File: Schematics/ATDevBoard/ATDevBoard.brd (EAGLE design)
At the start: 75.9 x 57.1 mm, 42 parts, among them U1 TINY85-20-DIP

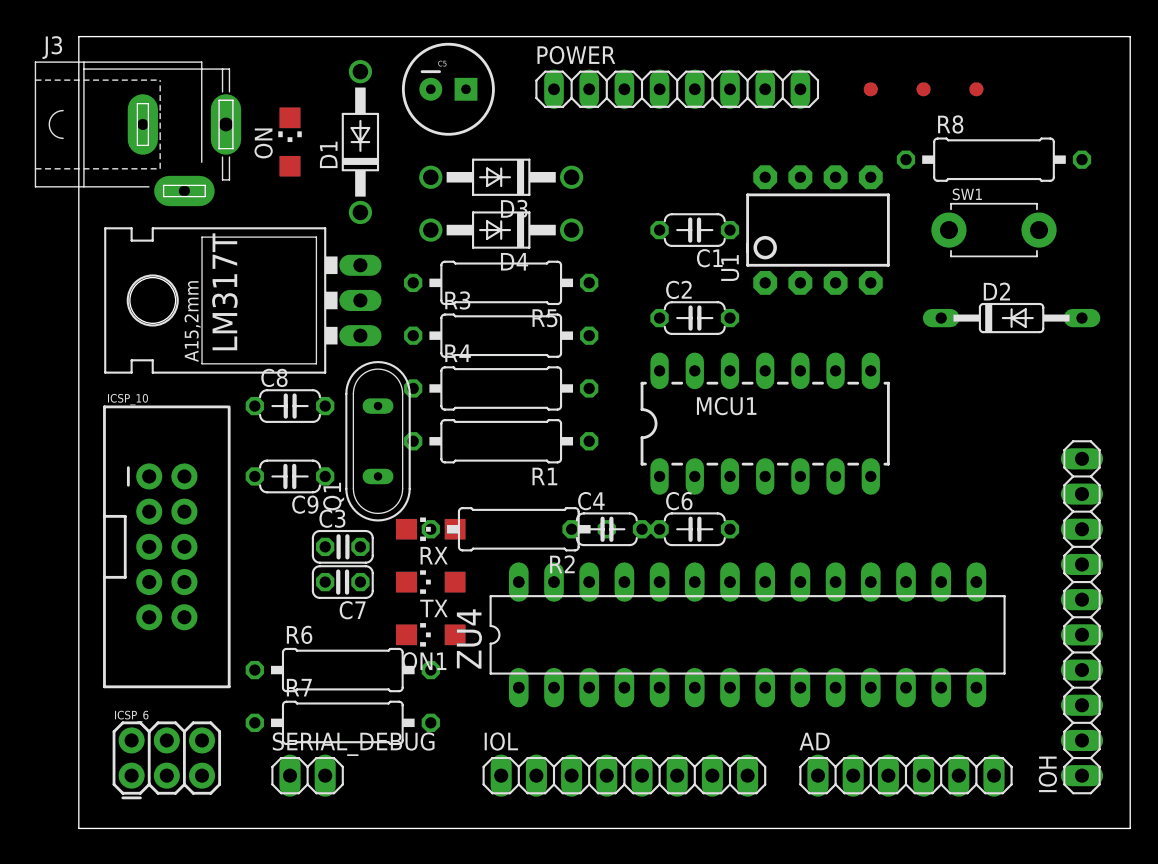
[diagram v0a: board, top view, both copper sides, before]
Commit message: Added vaule for regulator resistors, first routed version of brd. Added pdfs for brd and schematic.
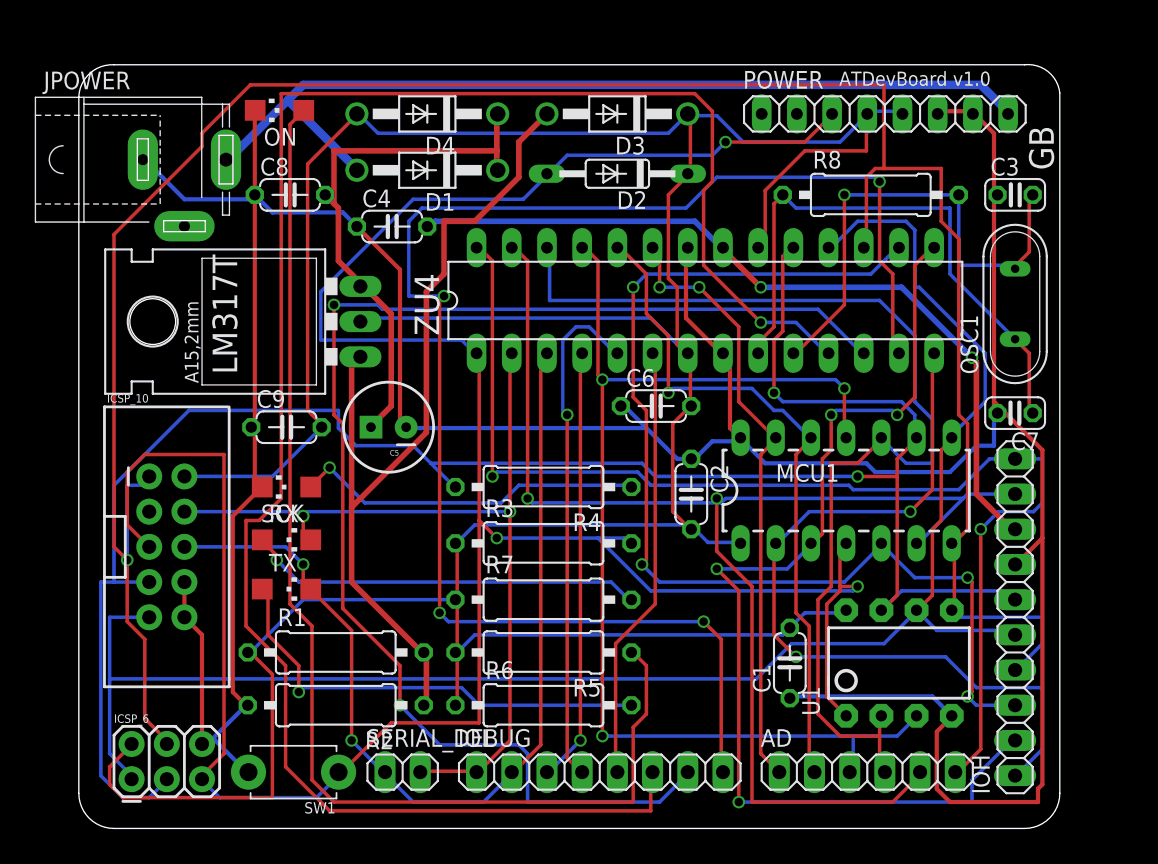
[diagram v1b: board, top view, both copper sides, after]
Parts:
- removed FD1, FD2, FD3: FIDUCIALMOUNT, SmartPrj:FIDUCIA-MOUNT
- removed J3: (no value), con-jack:SPC4077
- removed ON1: BLUE, led:CHIPLED_1206
- removed Q1: (no value), special:QS
- added JPOWER: (no value), con-jack:SPC4077
- added OSC1: (no value), special:QS
- added SCK: BLUE, led:CHIPLED_1206
- R1: value (none) -> 5K6
- R2: value 1M -> 10K
- R4: value (none) -> 1K
- R8: value 1K -> 1M
- moved SW1 63.9 mm to (15.5, 4.06), turned to 180 degrees
- moved C3 54.8 mm to (67.6, 45.7)
- moved C7 50.0 mm to (67.6, 30.0)
- moved C1 32.0 mm to (51.3, 11.9), turned to 90 degrees
- moved U1 31.8 mm to (59.2, 11.9)
- moved D2 30.3 mm to (38.9, 47.2), turned to 180 degrees
- moved R5 26.8 mm to (33.5, 12.7)
- moved C4 26.8 mm to (22.6, 43.4)
- moved C5 24.8 mm to (22.4, 29.0), turned to 180 degrees
- moved ZU4 24.3 mm to (45.2, 38.1)
- moved R1 19.4 mm to (18.5, 12.7), turned to 0 degrees
- moved R2 18.3 mm to (18.5, 8.89)
- moved R7 17.0 mm to (33.5, 16.5)
- moved R3 15.3 mm to (33.5, 20.6)
- moved C8 15.2 mm to (15.2, 45.7)
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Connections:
- net +3V3: now also R1.1, R5.2, R6.1; no longer R4.1, R6.2, R8.1
- net GND: now also JPOWER.1, R2.2, SCK.C; no longer J3.1, ON1.C, R1.2
- net N$1: now also R1.2, R2.1; no longer R1.1, R4.2
- net N$3: now also R5.1; no longer R6.1
- net N$35: now also R7.2; no longer R8.2
- net N$36: now also R6.2; no longer R7.2
- net N$4: now also R4.1, SCK.A; no longer ON1.A, R5.1
- net SCK: now also R4.2; no longer R5.2
- net VIN: now also JPOWER.3; no longer J3.3
- net XTAL1: now also OSC1.1, R8.1; no longer Q1.1, R2.1
- net XTAL2: now also OSC1.2, R8.2; no longer Q1.2, R2.2
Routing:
- net +3V3: track 0.00 -> 258.4 mm
- net GND: track 0.00 -> 250.8 mm
- net RESET: track 0.00 -> 191.8 mm, vias 0 -> 3
- net MOSI: track 0.00 -> 167.9 mm, vias 0 -> 1
- net SCK: track 0.00 -> 142.1 mm, vias 0 -> 2
- net IO5: track 0.00 -> 136.5 mm, vias 0 -> 1
- net MISO: track 0.00 -> 122.5 mm
- net IO7: track 0.00 -> 110.2 mm, vias 0 -> 4
- net IO6: track 0.00 -> 97.2 mm, vias 0 -> 2
- net AD4: track 0.00 -> 95.3 mm, vias 0 -> 2
- net AD5: track 0.00 -> 85.2 mm, vias 0 -> 2
- net N$3: track 0.00 -> 84.9 mm
- net AD2: track 0.00 -> 83.4 mm, vias 0 -> 3
- net SS: track 0.00 -> 79.7 mm, vias 0 -> 4
- net AD3: track 0.00 -> 77.9 mm
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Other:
- board size 75.9 x 57.1 mm -> 70.8 x 55.1 mm
- board text added: "ATDevBoard v1.0"
- board text added: "GB"

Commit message: Fixed packages for some resistors, replaced 1N4004 with 1N4007 diodes
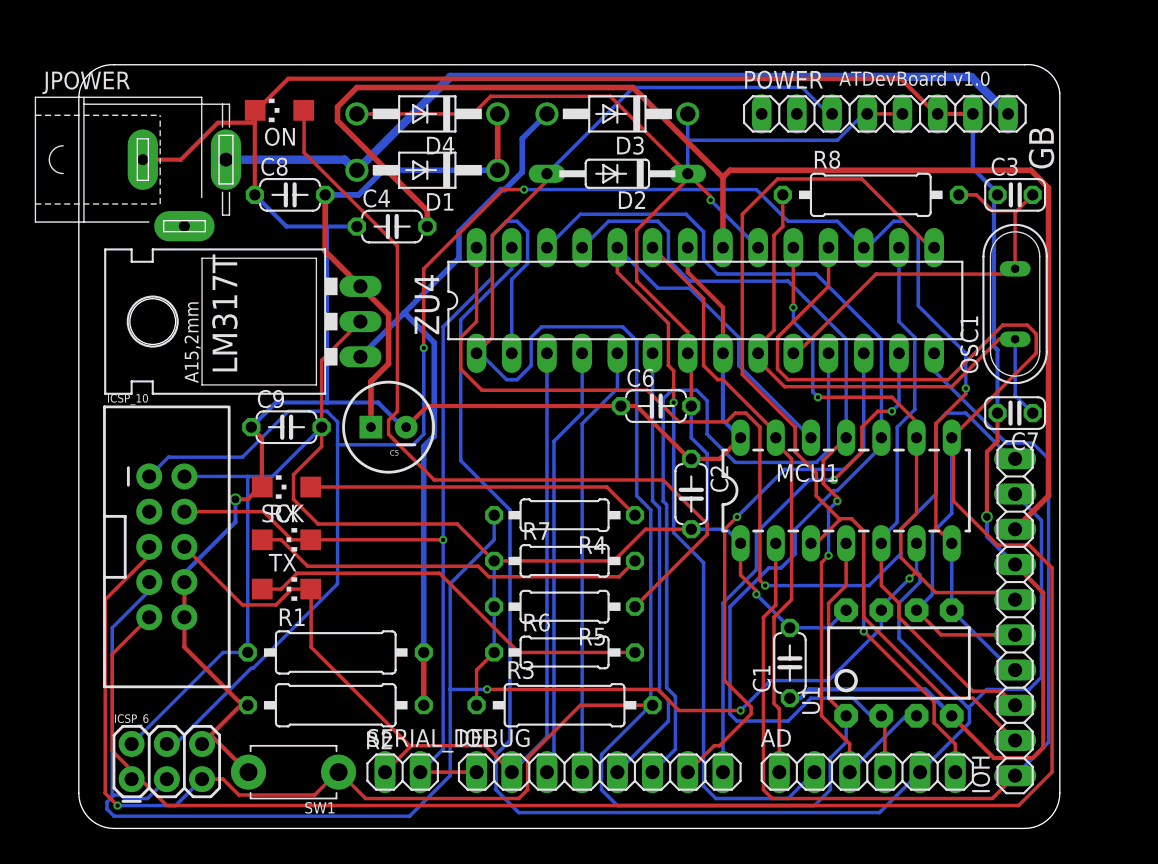
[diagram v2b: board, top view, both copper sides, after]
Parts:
- D3, D4: value 1N4004 -> 1N4007
- R4, R5, R6, R7: device rcl:0309/12 -> rcl:0207/10
- moved R3 11.8 mm to (35.1, 8.89)
- moved R6 4.10 mm to (35.1, 12.7)
- moved R5 3.64 mm to (35.1, 16.0)
- moved R7 3.18 mm to (35.1, 19.3)
- moved R4 2.54 mm to (35.1, 22.6)
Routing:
- net IO5: track 136.5 -> 51.1 mm, vias 1 -> 0
- net IO7: track 110.2 -> 37.1 mm, vias 4 -> 2
- net +3V3: track 258.4 -> 192.7 mm, vias 0 -> 2
- net IO6: track 97.2 -> 39.8 mm, vias 2 -> 1
- net MISO: track 122.5 -> 172.7 mm
- net SS: track 79.7 -> 39.7 mm, vias 4 -> 0
- net AREF: track 57.5 -> 97.3 mm, vias 2 -> 0
- net MOSI: track 167.9 -> 140.3 mm, vias 1 -> 3
- net N$3: track 84.9 -> 60.2 mm
- net AD1: track 49.1 -> 71.4 mm
- net AD4: track 95.3 -> 116.0 mm, vias 2 -> 0
- net AD2: track 83.4 -> 64.7 mm, vias 3 -> 2
- net IO0: track 61.2 -> 77.0 mm, vias 2 -> 1
- net IO8: track 57.6 -> 73.3 mm, vias 2 -> 0
- net N$1: track 63.5 -> 52.8 mm
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
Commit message: Fixed some components package with buy info, revisited board layout.
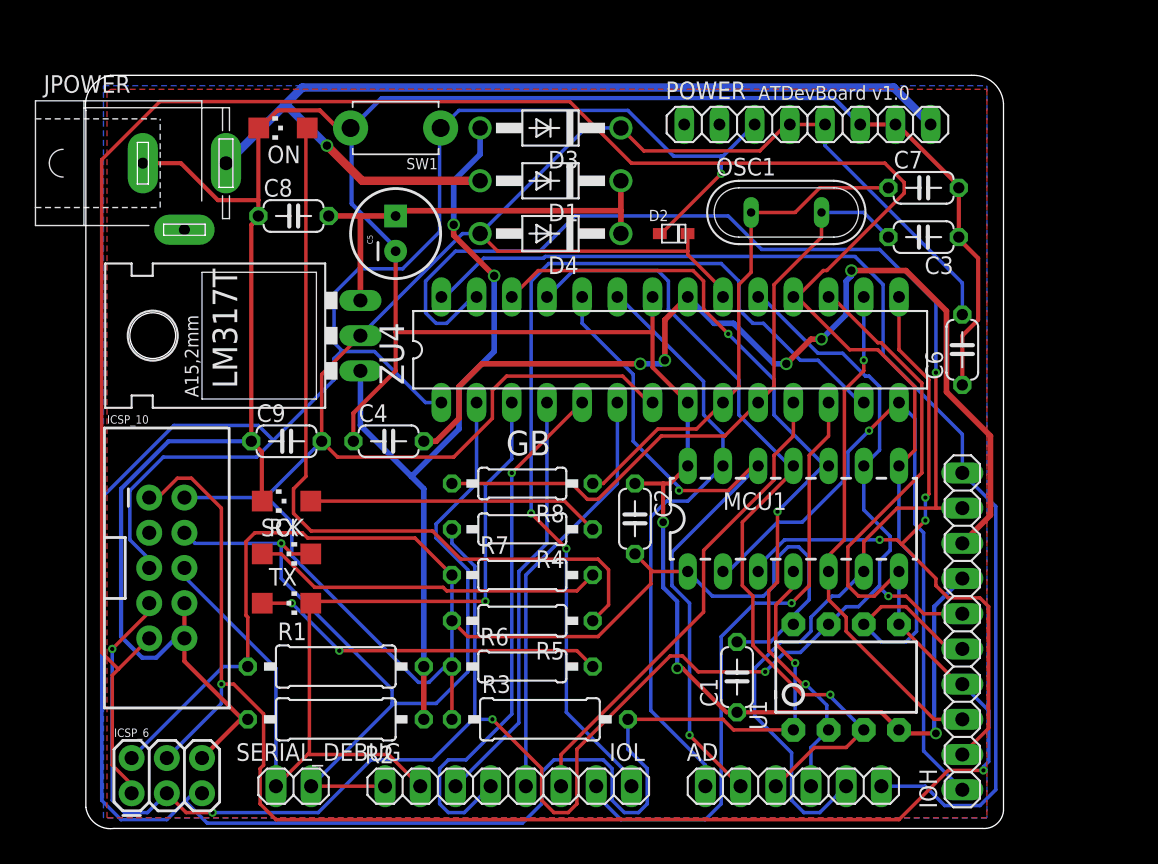
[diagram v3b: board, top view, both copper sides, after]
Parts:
- C3, C7: device SmartPrj:C025-024X044 -> SmartPrj:C050-024X044
- D2: device diode:DO35-10 -> adafruit:SOD-323F
- MCU1: value ATTINY84ATTINY84-20PU -> ATTINY84-20PU
- R8: device rcl:0309/12 -> rcl:0207/10
- U1: value TINY85-20-DIP -> TINY85-DIP
- moved SW1 47.1 mm to (22.9, 50.5)
- moved R8 32.7 mm to (32.0, 24.9), turned to 180 degrees
- moved C6 22.5 mm to (63.8, 34.5), turned to 90 degrees
- moved OSC1 17.8 mm to (51.1, 44.5), turned to 0 degrees
- moved C7 17.5 mm to (61.0, 46.2), turned to 0 degrees
- moved C4 15.5 mm to (22.4, 27.9)
- moved C5 14.0 mm to (22.9, 42.9), turned to 90 degrees
- moved D4 12.4 mm to (34.0, 42.9)
- moved D1 8.92 mm to (34.0, 46.7)
- moved SERIAL_DEBUG 7.94 mm to (15.5, 3.05)
- moved C3 7.27 mm to (61.0, 42.7), turned to 180 degrees
- moved IOL 6.68 mm to (31.0, 3.05)
- moved D2 5.93 mm to (42.9, 42.9), turned to 0 degrees
- moved POWER 5.64 mm to (52.6, 50.8)
- moved AD 5.43 mm to (51.6, 3.05)
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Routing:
- net +3V3: track 192.7 -> 241.1 mm, vias 2 -> 0
- net IO7: track 37.1 -> 69.3 mm
- net AREF: track 97.3 -> 71.6 mm, vias 0 -> 5
- net IO8: track 73.3 -> 48.6 mm, vias 0 -> 1
- net AD1: track 71.4 -> 51.1 mm, vias 1 -> 2
- net AD3: track 78.8 -> 59.8 mm, vias 0 -> 3
- net XTAL2: track 29.0 -> 46.6 mm
- net IO9: track 67.6 -> 51.1 mm, vias 0 -> 3
- net IO5: track 51.1 -> 34.6 mm
- net RESET: track 191.5 -> 207.0 mm, vias 1 -> 2
- net AD4: track 116.0 -> 100.6 mm, vias 0 -> 1
- net IO0: track 77.0 -> 66.4 mm
- net VIN: track 60.6 -> 70.5 mm, vias 0 -> 1
- net SCK: track 147.0 -> 137.8 mm
- net GND: track 248.3 -> 257.4 mm, vias 2 -> 3
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- added copper zone on layer 1, net GND
- added copper zone on layer 16, net GND
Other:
- board size 70.8 x 55.1 mm -> 66.2 x 54.4 mm

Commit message: Added micro USB, trimmer and PTC fuse
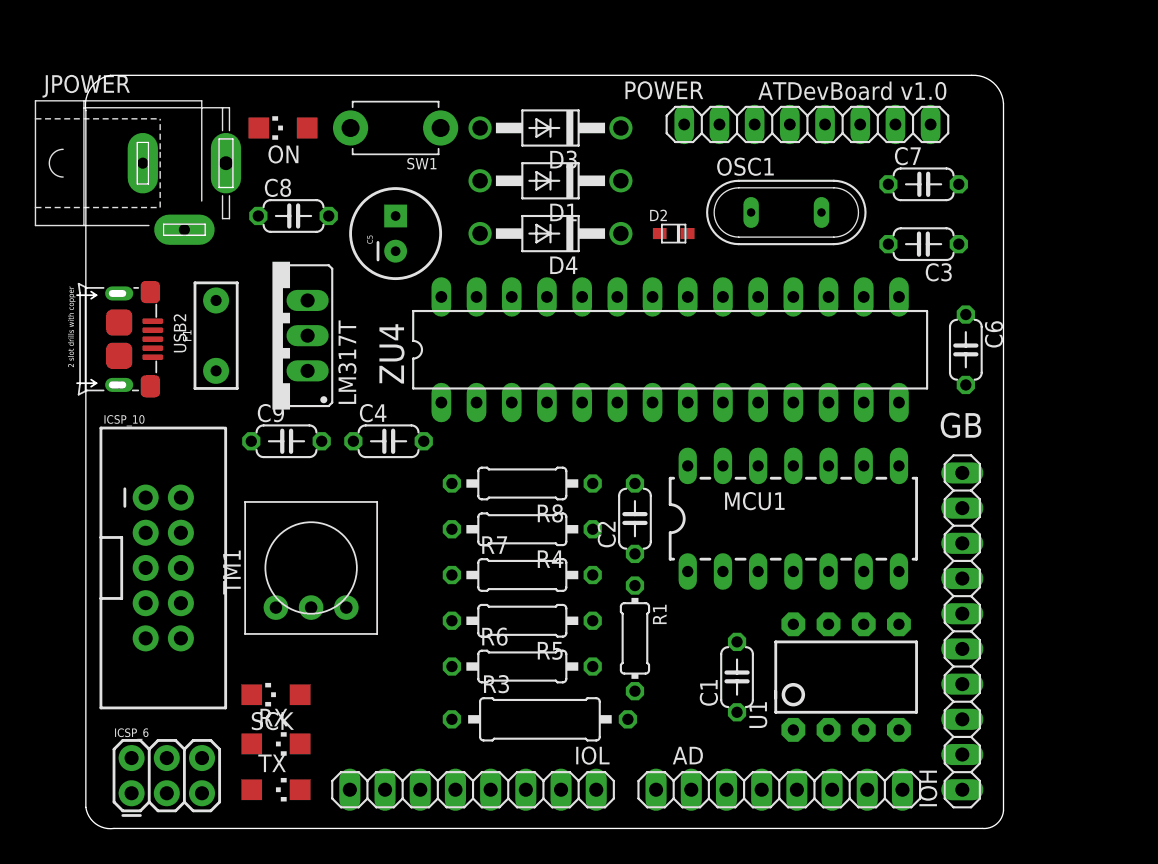
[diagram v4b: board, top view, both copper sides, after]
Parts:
- removed R2: 10K, rcl:0309/12
- removed SERIAL_DEBUG: 2x1F-H8.5, pinhead:1X02
- added F1: 72V/0.25A, SparkFun-Fuses:PTH
- added TM1: (no value), adafruit:TRIM-3386
- added USB2: 10118193-0001LF, Seeed-OPL-Connector:MICRO-USB5+6P-SMD-0.65-B
- AD: value 6x1F-H8.5 -> 8x1F-H8.5; device pinhead:1X06 -> pinhead:1X08
- LM317T: device v-reg:317TL -> v-reg:317TS
- R1: value 5K6 -> 220; device rcl:0309/12 -> rcl:0204/7
- moved R1 21.7 mm to (40.1, 13.7), turned to 270 degrees
- moved SCK 14.0 mm to (14.2, 9.65)
- moved RX 13.7 mm to (14.2, 6.10)
- moved TX 13.5 mm to (14.2, 2.79)
- moved IOL 2.55 mm to (28.4, 2.79)
- moved LM317T 2.54 mm to (14.0, 35.6)
- moved AD 1.05 mm to (50.5, 2.79)
- moved C3 0.51 mm to (61.0, 42.2)
- moved ICSP_10 0.25 mm to (6.10, 18.8)
- moved C6 0.25 mm to (64.0, 34.5), turned to 270 degrees
- moved C7 0.25 mm to (61.0, 46.5)
- turned C2 to 90 degrees
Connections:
- new net N$5: F1.P$1, USB2.1
- net GND: now also TM1.1, USB2.5; no longer R2.2
- net IO0: now also AD.8; no longer SERIAL_DEBUG.2
- net IO1: now also AD.7; no longer SERIAL_DEBUG.1
- net N$1: now also TM1.3; no longer R2.1
- net N$2: now also F1.P$2
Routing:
- net GND: track 257.4 -> 0.00 mm, vias 3 -> 0
- net +3V3: track 241.1 -> 0.00 mm
- net RESET: track 207.0 -> 0.00 mm, vias 2 -> 0
- net MISO: track 167.5 -> 0.00 mm
- net MOSI: track 139.2 -> 0.00 mm, vias 2 -> 0
- net SCK: track 137.8 -> 0.00 mm, vias 5 -> 0
- net AD4: track 100.6 -> 0.00 mm, vias 1 -> 0
- net AD5: track 83.1 -> 0.00 mm
- net AREF: track 71.6 -> 0.00 mm, vias 5 -> 0
- net VIN: track 70.5 -> 0.00 mm, vias 1 -> 0
- net IO1: track 69.6 -> 0.00 mm, vias 1 -> 0
- net IO7: track 69.3 -> 0.00 mm, vias 2 -> 0
- net IO0: track 66.4 -> 0.00 mm, vias 1 -> 0
- net AD2: track 60.5 -> 0.00 mm, vias 1 -> 0
- net AD3: track 59.8 -> 0.00 mm, vias 3 -> 0
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- removed copper zone on layer 1, net GND
- removed copper zone on layer 16, net GND

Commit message: Added plated slot for DC plug, new device for micro USB connector, updated partlist
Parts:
- removed USB2: 10118193-0001LF, Seeed-OPL-Connector:MICRO-USB5+6P-SMD-0.65-B
- added USB1: ZX62-B-5PA, Seeed-Connector:MICRO-USB5+6P-SMD-0.65-AB
- JPOWER: device con-jack:SPC4077 -> con-jack-plated-slots:SPC4077
- moved C6 34.3 mm to (30.7, 26.4), turned to 0 degrees
- moved R8 10.5 mm to (36.6, 15.5), turned to 270 degrees
- moved C2 4.34 mm to (38.6, 26.4), turned to 0 degrees
- moved C1 4.20 mm to (45.7, 14.7), turned to 180 degrees
- moved R3 4.02 mm to (29.5, 6.60)
- moved R4 4.02 mm to (28.2, 20.3)
- moved R5 4.02 mm to (28.2, 13.7)
- moved R6 4.02 mm to (28.2, 10.4)
- moved R7 4.02 mm to (28.2, 17.0)
- moved C9 1.55 mm to (14.7, 26.4)
- moved C4 1.52 mm to (22.4, 26.4)
- moved TM1 1.05 mm to (16.5, 17.8)
- moved R1 0.51 mm to (40.1, 14.2), turned to 90 degrees
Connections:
- removed net N$5: F1.P$1, USB2.1
- new net VBUS: F1.P$1, USB1.1
- net GND: now also USB1.5; no longer USB2.5
- net N$2: now also D1.A, JPOWER.3; no longer C5.1, C8.2, D1.C, D4.C, F1.P$2, LM317T.3
- net VIN: now also C5.1, C8.2, D1.C, D4.C, F1.P$2, LM317T.3; no longer D1.A, JPOWER.3
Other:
- board text added: "Slot drills with copper"

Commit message: Fixed package for trimmer
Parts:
- F1: value 72V/0.25A -> 90V/0.5A
- TM1: value (none) -> 2K; device adafruit:TRIM-3386 -> bourns:3362R
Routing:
- net GND: track 0.00 -> 224.3 mm, vias 0 -> 3
- net +3V3: track 0.00 -> 215.8 mm, vias 0 -> 2
- net RESET: track 0.00 -> 178.9 mm, vias 0 -> 2
- net SCK: track 0.00 -> 143.9 mm, vias 0 -> 4
- net MOSI: track 0.00 -> 141.2 mm, vias 0 -> 2
- net MISO: track 0.00 -> 140.1 mm, vias 0 -> 2
- net AREF: track 0.00 -> 122.2 mm
- net IO1: track 0.00 -> 109.2 mm, vias 0 -> 2
- net IO0: track 0.00 -> 103.4 mm, vias 0 -> 1
- net AD5: track 0.00 -> 99.0 mm
- net AD3: track 0.00 -> 89.6 mm, vias 0 -> 6
- net N$1: track 0.00 -> 80.7 mm
- net AD4: track 0.00 -> 78.9 mm, vias 0 -> 2
- net AD2: track 0.00 -> 65.5 mm, vias 0 -> 5
- net VIN: track 0.00 -> 62.3 mm, vias 0 -> 1
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
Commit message: Replaced Dc plug with component in CuSTOM_GB library
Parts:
- JPOWER: device con-jack-plated-slots:SPC4077 -> CuSTOM_GB:SPC4077
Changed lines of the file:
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@@
 <attribute name="NAME" x="35.7378" y="4.6228" size="1.27" layer="25" ratio="10"/>
 </element>
-<element name="JPOWER" library="con-jack-plated-slots" package="SPC4077" value="" x="7.62" y="48.006">
+<element name="JPOWER" library="CuSTOM_GB" package="SPC4077" value="" x="7.62" y="48.006">
 <attribute name="OC_FARNELL" value="unknown" x="7.62" y="48.006" size="1.778" layer="27" display="off"/>
 <attribute name="OC_NEWARK" value="unknown" x="7.62" y="48.006" size="1.778" layer="27" display="off"/>
@@
 <wire x1="7.112" y1="38.862" x2="7.112" y2="37.846" width="0.4064" layer="1"/>
 <wire x1="7.112" y1="37.846" x2="6.096" y2="36.83" width="0.4064" layer="1"/>
-<wire x1="6.096" y1="36.83" x2="5.669" y2="36.86" width="0" layer="19" extent="1-16"/>
+<wire x1="6.096" y1="36.83" x2="5.669" y2="36.86" width="0" layer="19" extent="1-1"/>
 </signal>
 </signals>
